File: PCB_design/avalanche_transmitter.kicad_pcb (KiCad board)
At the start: 2 copper layers, 8 parts, among them J1 Conn_01x07_Pin, Q1 2N3904, U1 74HC00

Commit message: edited layout
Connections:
- J1 pad 2: unconnected-(J1-Pin_2-Pad2) -> +6V
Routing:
- net +6V: track 0.00 -> 67.6 mm, vias 0 -> 3
- net Net-(J1-Pin_4): track 64.9 -> 58.5 mm
- net Net-(J1-Pin_1): track 61.9 -> 58.9 mm

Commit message: Add files via upload
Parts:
- removed J1: Conn_01x07_Pin, Connector_PinHeader_2.54mm:PinHeader_1x07_P2.54mm_Vertical
- added 100%: RED_LED_100, LED_THT:LED_D5.0mm, F.Cu at (38.3, 87.3)
- added 25%: RED_LED_25, LED_THT:LED_D5.0mm, F.Cu at (38.6, 118.2)
- added 50%: RED_LED_50, LED_THT:LED_D5.0mm, F.Cu at (38.5, 107.7)
- added 6V: PinHeader_1x01_P1.00mm_Vertical, Connector_PinHeader_1.00mm:PinHeader_1x01_P1.00mm_Vertical, F.Cu at (63.0, 119.3)
- added 75%: RED_LED_75, LED_THT:LED_D5.0mm, F.Cu at (38.4, 97.4)
- added GND: PinHeader_1x01_P1.00mm_Vertical, Connector_PinHeader_1.00mm:PinHeader_1x01_P1.00mm_Vertical, F.Cu at (77.2, 119.2)
- added R1: R_Small, Resistor_THT:R_Axial_DIN0204_L3.6mm_D1.6mm_P7.62mm_Horizontal, F.Cu at (45.6, 115.7)
- added R2: R_Small, Resistor_THT:R_Axial_DIN0204_L3.6mm_D1.6mm_P7.62mm_Horizontal, F.Cu at (45.5, 105.2)
- added R3: R_Small, Resistor_THT:R_Axial_DIN0204_L3.6mm_D1.6mm_P7.62mm_Horizontal, F.Cu at (45.6, 94.8)
- added R4: R_Small, Resistor_THT:R_Axial_DIN0204_L3.6mm_D1.6mm_P7.62mm_Horizontal, F.Cu at (45.6, 84.8)
- added R5: R_Small, Resistor_THT:R_Axial_DIN0204_L3.6mm_D1.6mm_P7.62mm_Horizontal, F.Cu at (45.5, 75.3)
- added R6: R_Small, Resistor_THT:R_Axial_DIN0204_L3.6mm_D1.6mm_P7.62mm_Horizontal, F.Cu at (58.4, 66.1)
- added SI_5351A: SI_5351A, Connector_PinHeader_1.00mm:PinHeader_1x07_P1.00mm_Vertical, F.Cu at (74.7, 60.4)
- added TRANSMITTING: GREEN_LED, LED_THT:LED_D5.0mm, F.Cu at (38.1, 73.9)
- moved C2 131.9 mm to (41.4, 41.0), turned to -90 degrees
- moved U3 130.6 mm to (63.4, 28.6), turned to 90 degrees
- moved C3 126.1 mm to (47.7, 40.9), turned to -90 degrees
- moved RV1 119.1 mm to (42.5, 55.8), turned to 90 degrees
- moved AE1 116.1 mm to (54.0, 44.8), turned to 180 degrees
- moved U1 102.0 mm to (79.9, 44.0), turned to -90 degrees
- moved Q1 99.8 mm to (57.2, 57.4), turned to 90 degrees
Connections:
- AE1 pad 2: +3V0 -> 6V
- C2 pad 1: +3V0 -> 6V
- C3 pad 1: +3V0 -> 6V
- U1 pad 1: Net-(J1-Pin_1) -> si[0]
- U3 pad 1: +6V -> 6V
- U3 pad 10: unconnected-(U3-TX-Pad10) -> (no net)
- U3 pad 11: unconnected-(U3-RX-Pad11) -> (no net)
- U3 pad 12: unconnected-(U3-RST-Pad12) -> (no net)
- U3 pad 13: unconnected-(U3-9-Pad13) -> (no net)
- U3 pad 14: unconnected-(U3-10-Pad14) -> (no net)
- U3 pad 15: unconnected-(U3-11-Pad15) -> (no net)
- U3 pad 17: unconnected-(U3-13-Pad17) -> Net-(D5-K)
- U3 pad 18: unconnected-(U3-Ar-Pad18) -> (no net)
- U3 pad 19: unconnected-(U3-A0-Pad19) -> (no net)
- U3 pad 20: unconnected-(U3-A1-Pad20) -> (no net)
- U3 pad 21: unconnected-(U3-A2-Pad21) -> (no net)
- U3 pad 22: unconnected-(U3-A3-Pad22) -> (no net)
- U3 pad 23: Net-(J1-Pin_5) -> SDA
- U3 pad 24: Net-(J1-Pin_4) -> SCL
- U3 pad 3: unconnected-(U3-bus-Pad3) -> (no net)
- U3 pad 5: unconnected-(U3-8-Pad5) -> (no net)
- U3 pad 6: unconnected-(U3-Pad6) -> Net-(D4-K)
- U3 pad 7: unconnected-(U3-5-Pad7) -> Net-(D3-K)
- U3 pad 8: unconnected-(U3-4-Pad8) -> Net-(D2-K)
- U3 pad 9: unconnected-(U3-3-Pad9) -> Net-(D1-K)
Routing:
- net 6V: track 0.00 -> 144.6 mm
- net Net-(D1-K): track 0.00 -> 135.8 mm
- net Net-(D2-K): track 0.00 -> 121.3 mm
- net Net-(D3-K): track 0.00 -> 107.3 mm
- net +3V0: track 105.5 -> 0.00 mm, vias 2 -> 0
- net GND: track 103.9 -> 0.00 mm
- net Net-(D4-K): track 0.00 -> 93.3 mm
- net +6V: track 67.6 -> 0.00 mm, vias 3 -> 0
- net Net-(J1-Pin_1): track 58.9 -> 0.00 mm, vias 2 -> 0
- net Net-(J1-Pin_4): track 58.5 -> 0.00 mm
- net Net-(D5-K): track 0.00 -> 57.4 mm, vias 0 -> 1
- net Net-(J1-Pin_5): track 54.8 -> 0.00 mm
- net SCL: track 0.00 -> 40.8 mm
- net SDA: track 0.00 -> 39.3 mm
- net si[0]: track 0.00 -> 34.9 mm
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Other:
- board text added: "Avalanche Transmitter"

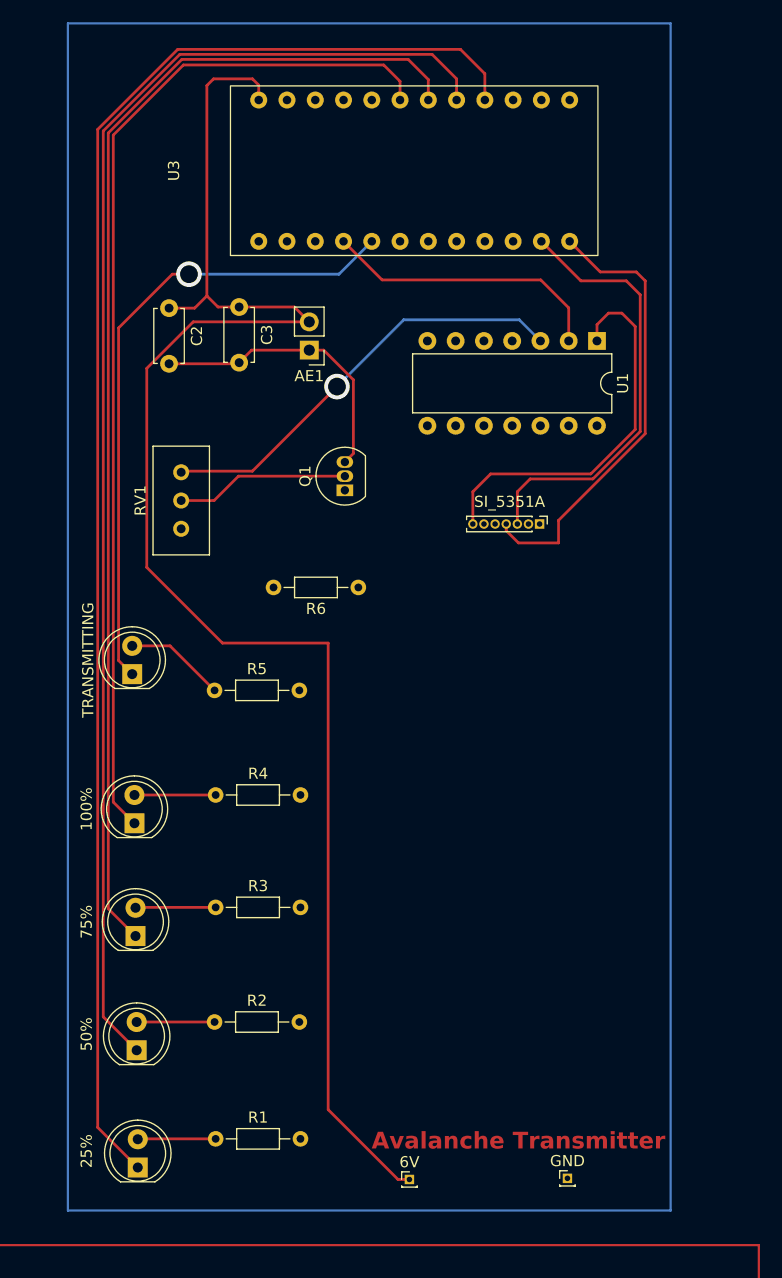
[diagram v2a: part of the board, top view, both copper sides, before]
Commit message: PCB updates
Added some vias, rerouted some things, changed the footprint for the SI
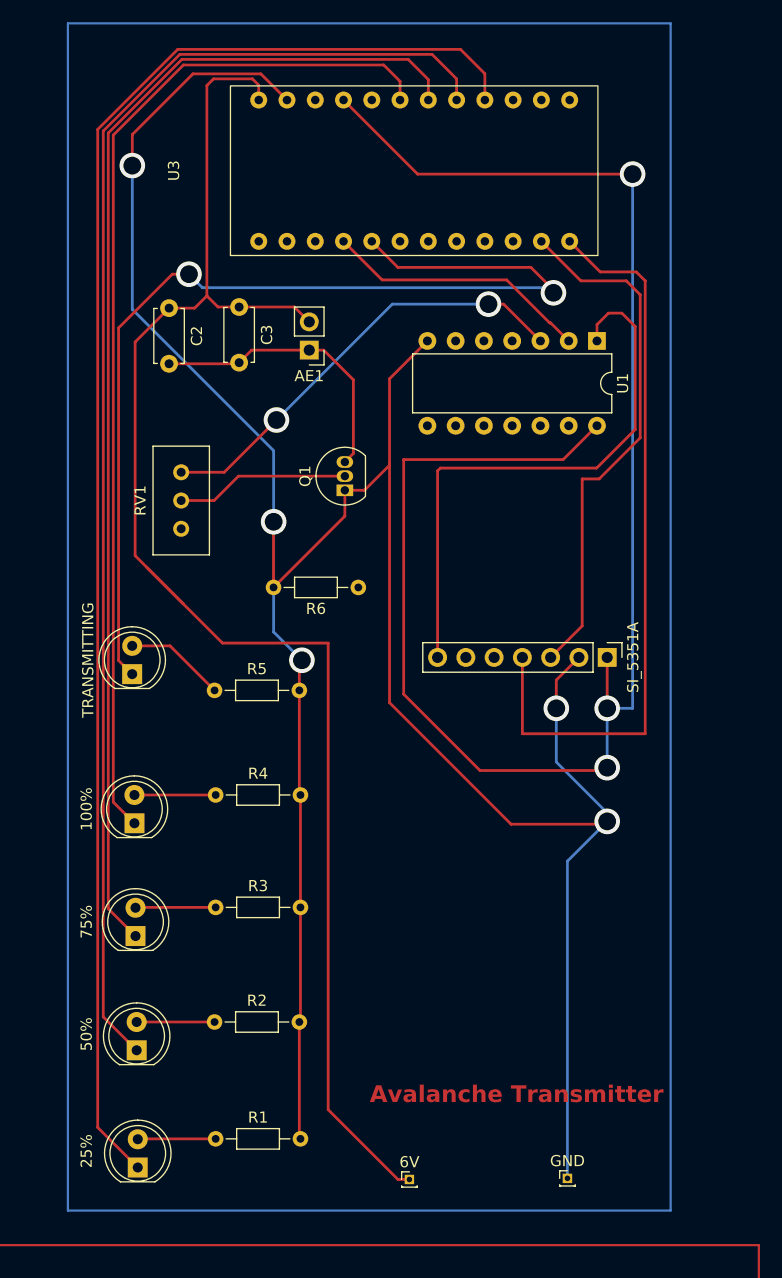
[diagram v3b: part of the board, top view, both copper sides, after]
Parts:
- SI_5351A: footprint Connector_PinHeader_1.00mm:PinHeader_1x07_P1.00mm_Vertical -> Connector_PinHeader_2.54mm:PinHeader_1x07_P2.54mm_Vertical
- moved SI_5351A 13.4 mm to (80.8, 72.4)
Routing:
- net GND: track 0.00 -> 245.9 mm, vias 0 -> 5
- net +3V0: track 0.00 -> 149.9 mm, vias 0 -> 3
- net Net-(D5-K): track 57.4 -> 91.6 mm, vias 1 -> 2
- net SCL: track 40.8 -> 66.9 mm
- net si[0]: track 34.9 -> 51.1 mm
- net SDA: track 39.3 -> 47.7 mm
- net 6V: track 144.6 -> 140.0 mm
- net Net-(U2-12): track 25.7 -> 23.9 mm
- net Net-(RV1-Pad1): track 38.7 -> 40.1 mm, vias 1 -> 2

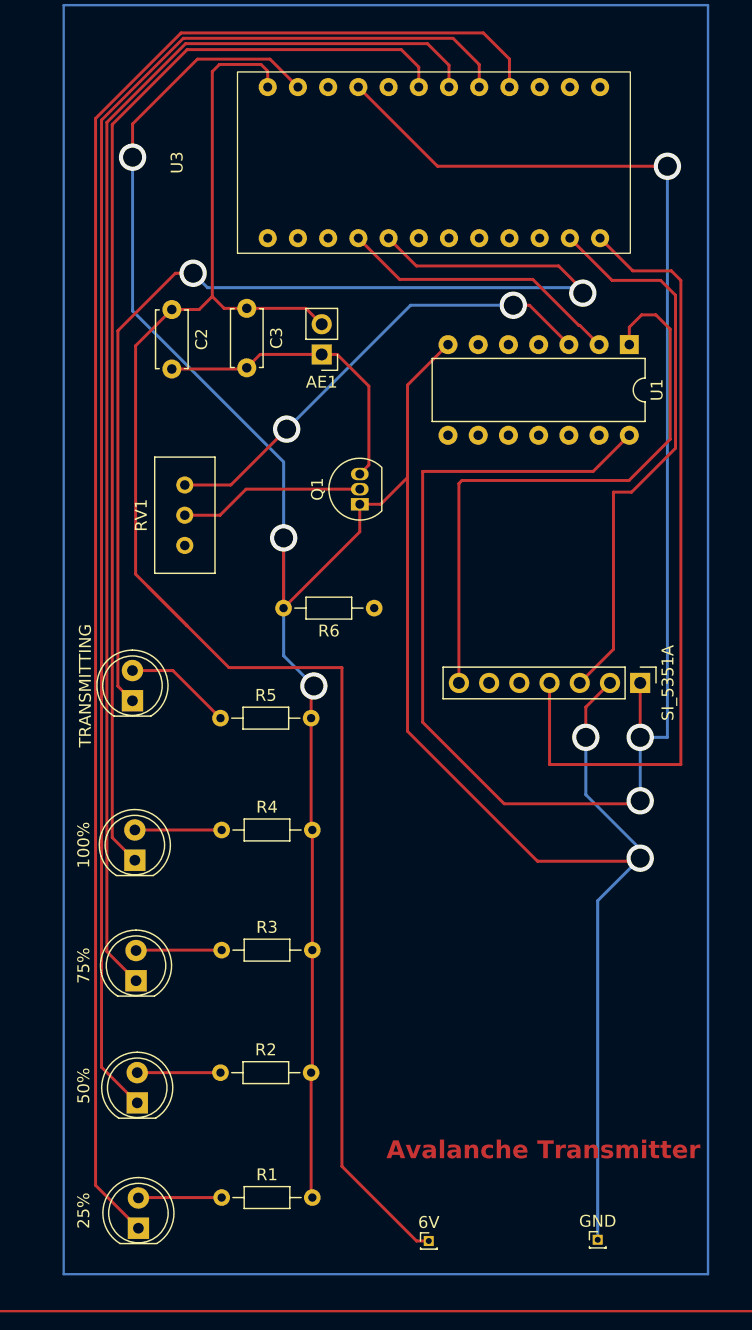
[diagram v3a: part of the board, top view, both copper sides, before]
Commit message: added series resistor to increase magfield
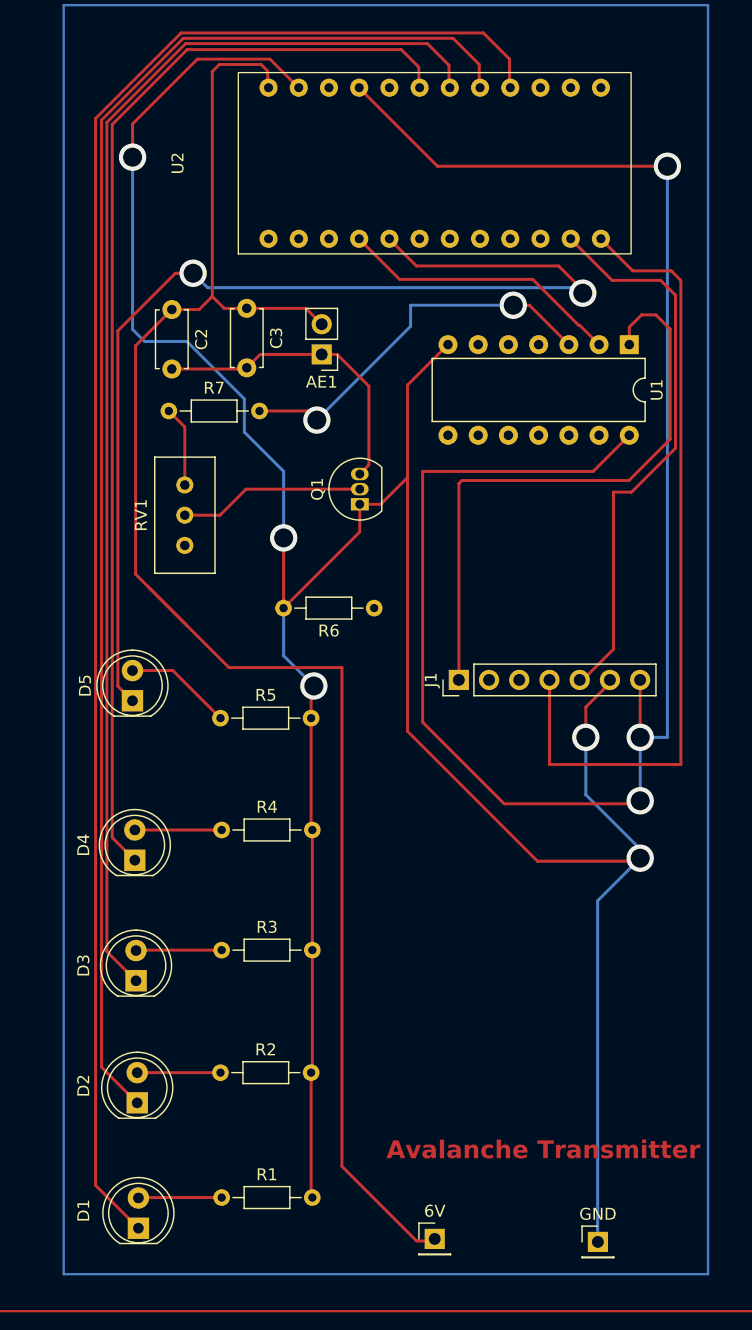
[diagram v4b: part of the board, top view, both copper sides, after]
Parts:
- removed the 6V at (63.0, 119.3)
- removed the GND at (77.2, 119.2)
- removed SI_5351A: SI_5351A, Connector_PinHeader_2.54mm:PinHeader_1x07_P2.54mm_Vertical
- removed U3: ~, ta:pro_mini
- added 6V: PinHeader_1x01_P2.54mm_Vertical, Connector_PinHeader_2.54mm:PinHeader_1x01_P2.54mm_Vertical, F.Cu at (63.5, 119.1)
- added GND: PinHeader_1x01_P2.54mm_Vertical, Connector_PinHeader_2.54mm:PinHeader_1x01_P2.54mm_Vertical, F.Cu at (77.2, 119.4)
- added J1: Conn_01x07_Pin, Connector_PinHeader_2.54mm:PinHeader_1x07_P2.54mm_Vertical, F.Cu at (65.5, 72.1)
- added R7: R_Small, Resistor_THT:R_Axial_DIN0204_L3.6mm_D1.6mm_P7.62mm_Horizontal, F.Cu at (41.1, 49.5)
- added U2: ~, ta:pro_mini, F.Cu at (63.5, 28.7)
- renumbered 25% to D1, 50% to D2, 75% to D3, 100% to D4, TRANSMITTING to D5
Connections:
- net 6V renamed +6V
- RV1 pad 1: Net-(RV1-Pad1) -> Net-(R7-Pad1)
- RV1 pad 3: unconnected-(RV1-Pad3) -> GND
- U1 pad 1: si[0] -> Net-(J1-Pin_1)
- U1 pad 3: Net-(RV1-Pad1) -> Net-(R7-Pad2)
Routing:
- net SCL: track 66.9 -> 0.00 mm
- net Net-(J1-Pin_4): track 0.00 -> 66.9 mm
- net si[0]: track 51.1 -> 0.00 mm
- net Net-(J1-Pin_1): track 0.00 -> 51.1 mm
- net SDA: track 47.7 -> 0.00 mm
- net Net-(J1-Pin_5): track 0.00 -> 47.7 mm
- net Net-(RV1-Pad1): track 40.1 -> 0.00 mm, vias 2 -> 0
- net Net-(R7-Pad2): track 0.00 -> 32.7 mm, vias 0 -> 2
- net Net-(R7-Pad1): track 0.00 -> 6.92 mm
- net GND: track 245.9 -> 248.0 mm

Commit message: finished PCB. ready for bens review
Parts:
- removed D1: RED_LED_25, LED_THT:LED_D5.0mm
- added 25%: RED_LED_25, LED_THT:LED_D5.0mm, F.Cu at (38.5, 118.1)
- added REF**: MountingHole_2.1mm, MountingHole:MountingHole_2.1mm, F.Cu at (34.6, 122.4)
- added REF**: MountingHole_2.1mm, MountingHole:MountingHole_2.1mm, F.Cu at (84.5, 17.4)
- added REF**: MountingHole_2.1mm, MountingHole:MountingHole_2.1mm, F.Cu at (35.0, 17.4)
- added REF**: MountingHole_2.1mm, MountingHole:MountingHole_2.1mm, F.Cu at (84.8, 122.4)
- added REF**: SW_PUSH-12mm, Button_Switch_THT:SW_PUSH-12mm, F.Cu at (64.5, 96.2)
- moved R6 26.4 mm to (74.6, 87.0)
- moved J1 8.37 mm to (63.0, 80.1)
- moved R7 3.72 mm to (44.7, 50.7)
- moved R5 2.75 mm to (45.5, 72.6)
- moved GND 1.94 mm to (77.7, 117.5)
- moved 6V 1.70 mm to (64.0, 117.5)
- moved R1 1.35 mm to (45.6, 117.0)
- moved R2 1.25 mm to (45.5, 106.4)
- moved R4 1.25 mm to (45.6, 86.0)
- renumbered D4 to 100%, D2 to 50%, D3 to 75%, D5 to TRANSMITTING
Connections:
- 100% pad 1: Net-(D4-K) -> Net-(D1-K)
- 50% pad 1: Net-(D2-K) -> Net-(D3-K)
- 6V pad 1: (no net) -> +6V
- 75% pad 1: Net-(D3-K) -> Net-(D2-K)
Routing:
- net GND: track 248.0 -> 0.42 mm, vias 5 -> 12
- net Net-(U2-8): track 0.00 -> 116.6 mm, vias 0 -> 1
- net +3V0: track 149.9 -> 78.8 mm, vias 3 -> 0
- net +6V: track 140.0 -> 190.0 mm, vias 0 -> 1
- net Net-(D4-K): track 93.3 -> 135.8 mm
- net Net-(D1-K): track 135.8 -> 93.3 mm
- net Net-(D5-K): track 91.6 -> 57.4 mm, vias 2 -> 1
- net Net-(J1-Pin_5): track 47.7 -> 66.0 mm
- net Net-(D3-K): track 107.3 -> 121.3 mm
- net Net-(D2-K): track 121.3 -> 107.3 mm
- net Net-(J1-Pin_1): track 51.1 -> 62.9 mm
- net Net-(R7-Pad2): track 32.7 -> 29.8 mm
- net Net-(J1-Pin_4): track 66.9 -> 68.3 mm
- net Net-(D5-A): track 9.06 -> 7.91 mm
- net Net-(R7-Pad1): track 6.92 -> 5.96 mm
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- added copper zone on B.Cu, net GND
- added copper zone on F.Cu, net GND
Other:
- board outline added: 55 x 110 mm
- board text added: "SI5351A"

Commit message: updated layout. ready for review again
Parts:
- Battery In (6V): renamed from 6V
- Trinket Pro Mini: renamed from U2
- Variable Cap: renamed from C2
- Variable Resistor: renamed from RV1
- moved Battery In (6V) 24.1 mm to (84.7, 105.1)
- moved GND 6.06 mm to (76.0, 111.7)
- renumbered U1 to 74HC00, AE1 to Antenna, C3 to Cap, J1 to SI5351A, Q1 to Transistor
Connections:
- Antenna pad 2: +6V -> +3V0
- Cap pad 1: +6V -> +3V0
- REF** pad 2: +6V -> +3V0
- Variable Cap pad 1: +6V -> +3V0
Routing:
- net +3V0: track 78.8 -> 148.8 mm, vias 0 -> 1
- net +6V: track 190.0 -> 122.6 mm
- net Net-(R7-Pad2): track 29.8 -> 33.8 mm
- net Net-(D5-K): track 57.4 -> 59.9 mm
- net GND: vias 12 -> 10
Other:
- board text added: "Avalanche Transmitter 457 kHz"
- board text added: "BATTERY"
- board text removed: "Avalanche Transmitter"
- board text removed: "SI5351A"
